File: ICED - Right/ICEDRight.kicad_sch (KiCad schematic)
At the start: 76 parts

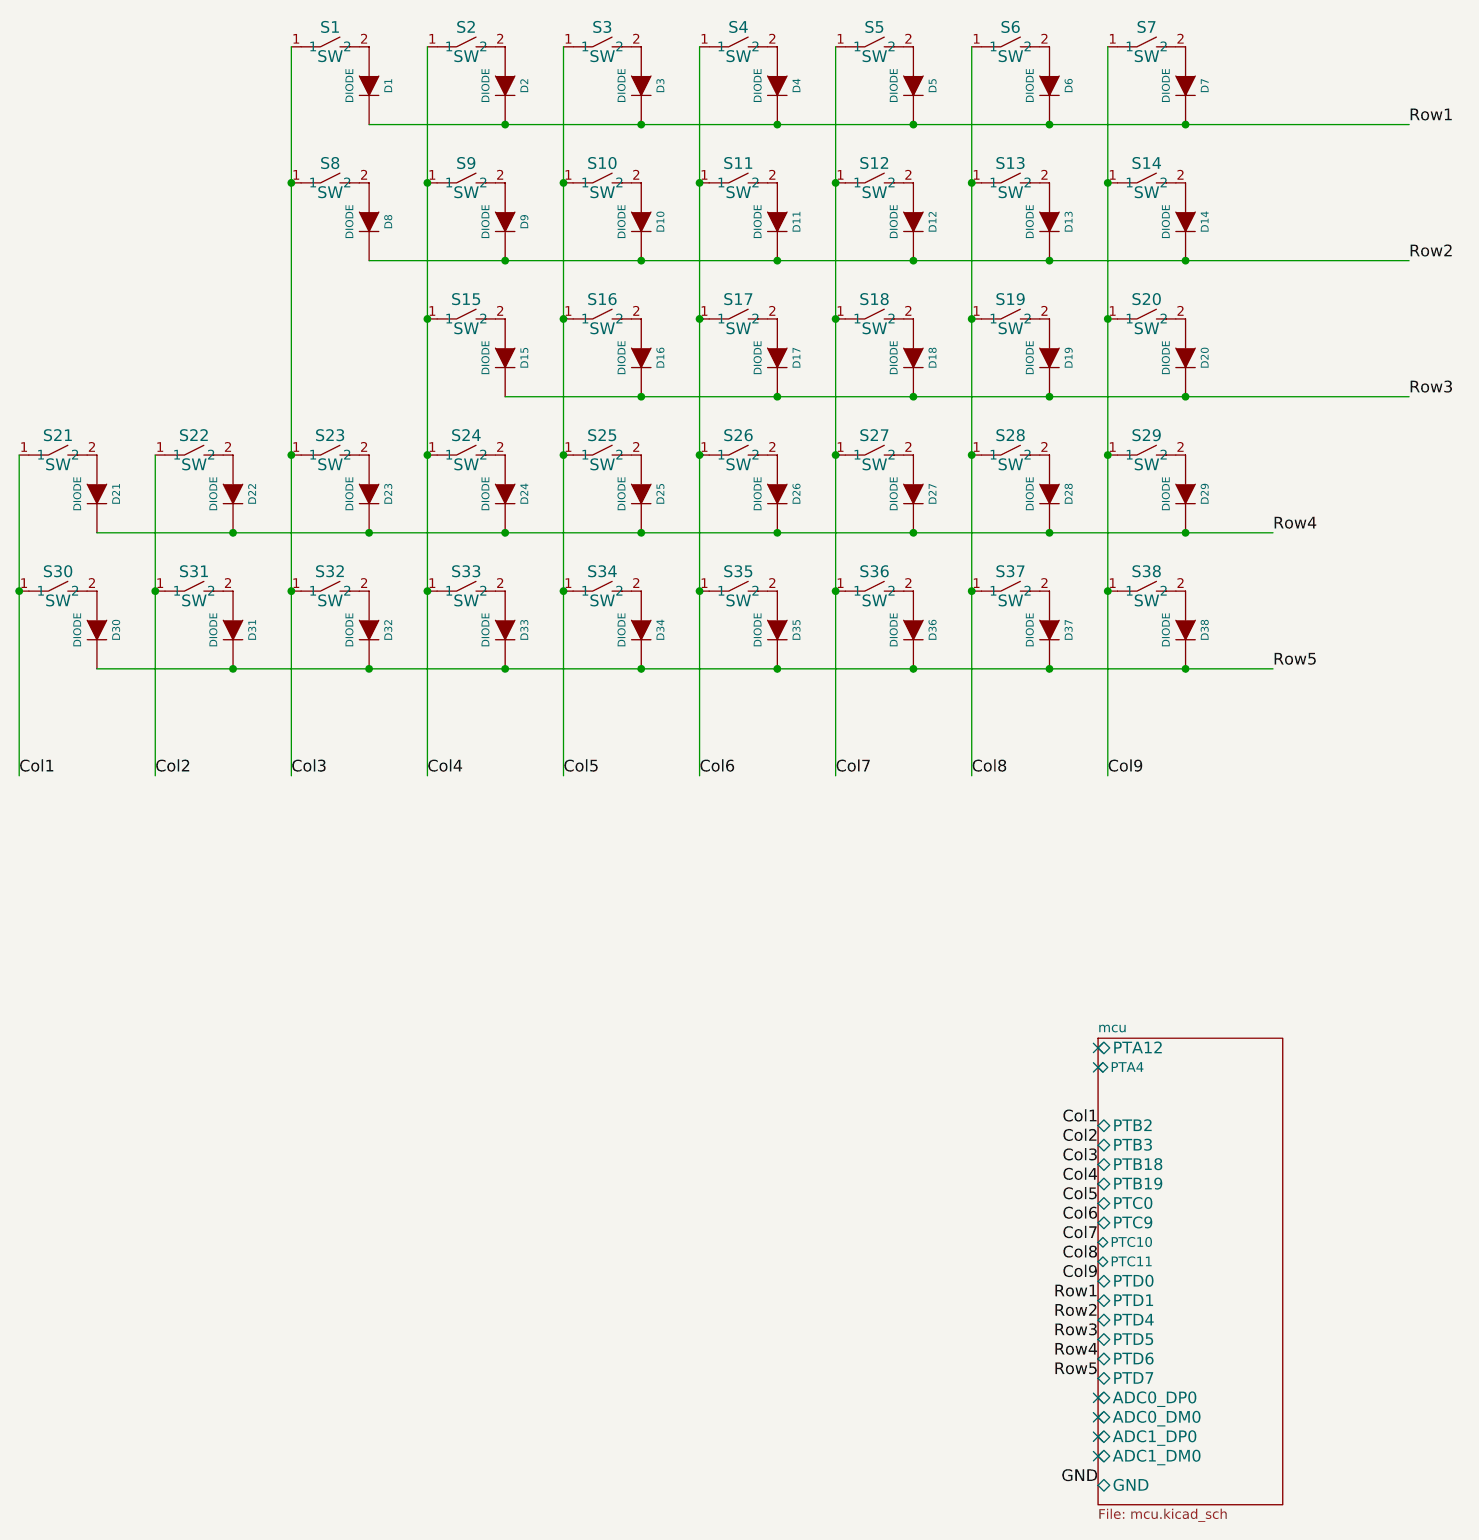
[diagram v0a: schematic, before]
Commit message: Upgrade project + Right changes
- Replace MXALPS sockets by Kailh Hot-swaps
- Replace the LED controller
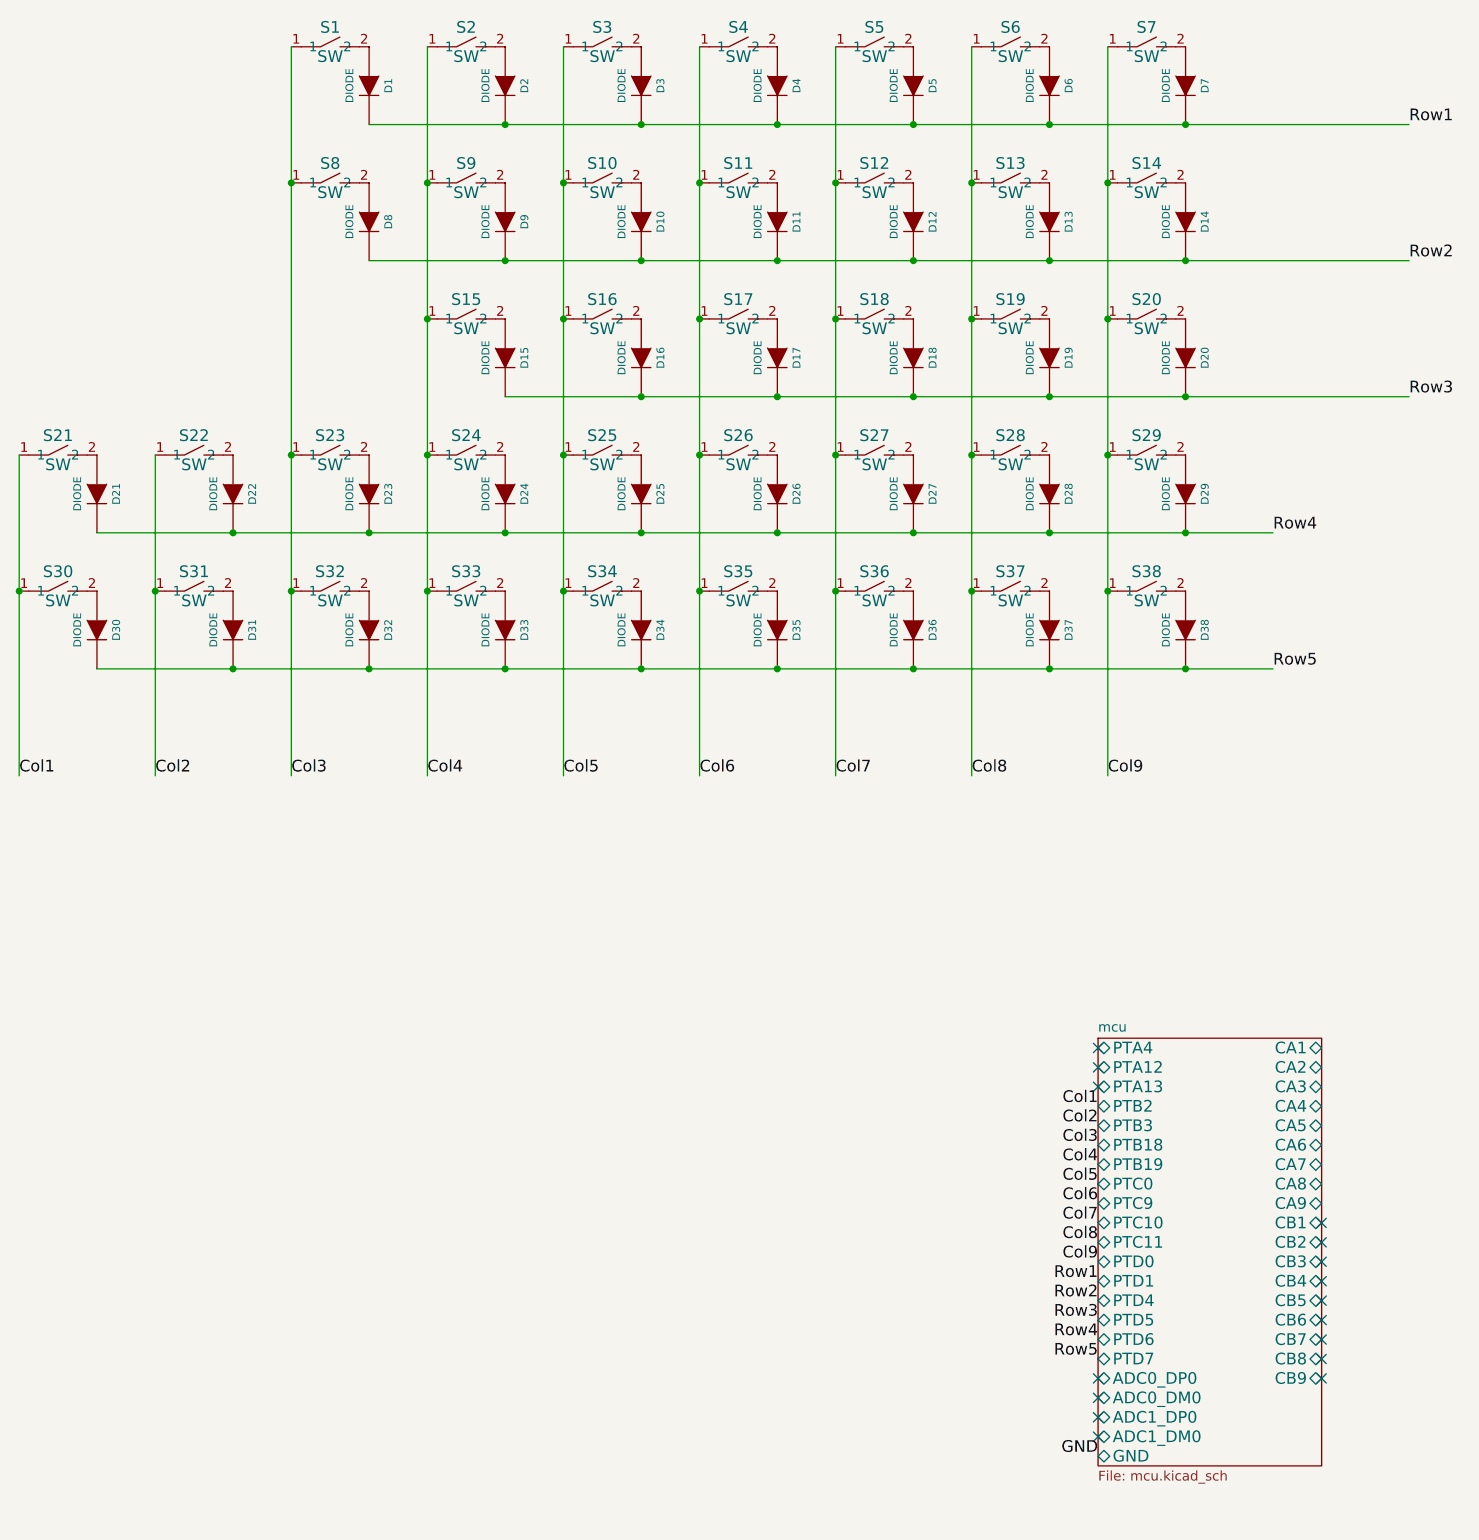
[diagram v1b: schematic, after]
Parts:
- D1, D10, D11, D12, D13, D14, D15, D16, D17, D18, D19, D2, D20, D21, D22, D23, D24, D25, D26, D27, D28, D29, D3, D30, D31, D32, D33, D34, D35, D36, D37, D38, D4, D5, D6, D7, D8, D9: footprint prettylib:1N4148 -> prettylib:SOT123-DIODE; symbol ICEDLeft:DIODE -> ICEDRight:DIODE
- S1, S10, S11, S12, S13, S14, S15, S16, S17, S18, S19, S2, S20, S21, S22, S23, S24, S25, S26, S27, S28, S29, S3, S30, S31, S32, S33, S34, S35, S36, S37, S38, S4, S5, S6, S7, S8, S9: symbol ICEDLeft:SW -> ICEDRight:SW
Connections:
- no-connect marks 6 -> 16
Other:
- sheet mcu ports: added CA1, CA2, CA3, CA4, CA5, CA6, CA7, CA8, CA9, CB1, CB2, CB3, CB4, CB5, CB6, CB7, CB8, CB9, PTA13; removed none
- title: ICED-L -> ICED-R
